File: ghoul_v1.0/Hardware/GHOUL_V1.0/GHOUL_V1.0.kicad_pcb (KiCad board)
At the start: 4 copper layers, 105.4 x 88.9 mm, 255 parts, among them M1 Motor_Servo, U1 Teensy4.1, U2 DS18S20, U3 Xbee, U4 TPS62133, U5 MS5607-02BA, U6 SAM-M8Q

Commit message: almost have V1.0 cleaned up
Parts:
- removed M1: Motor_Servo, Connector_JST:JST_EH_B4B-EH-A_1x04_P2.50mm_Vertical
- removed the REF** at (116.2, 69.2)
- removed REF**1, REF**10, REF**100, REF**101, REF**102, REF**103, REF**104, REF**105, REF**106, REF**107, REF**108, REF**109, REF**11, REF**110, REF**111, REF**112, REF**113, REF**114, REF**115, REF**117, REF**118, REF**119, REF**12, REF**120, REF**121, REF**122, REF**123, REF**125, REF**126, REF**127, REF**128, REF**129, REF**13, REF**130, REF**131, REF**133, REF**134, REF**135, REF**136, REF**137, REF**138, REF**139, REF**14, REF**140, REF**144, REF**145, REF**146, REF**147, REF**148, REF**149, REF**15, REF**150, REF**151, REF**152, REF**153, REF**154, REF**155, REF**156, REF**157, REF**158, REF**159, REF**16, REF**160, REF**161, REF**162, REF**163, REF**164, REF**165, REF**166, REF**167, REF**168, REF**169, REF**17, REF**170, REF**171, REF**172, REF**173, REF**174, REF**175, REF**176, REF**177, REF**178, REF**179, REF**18, REF**180, REF**181, REF**182, REF**183, REF**184, REF**185, REF**186, REF**187, REF**188, REF**189, REF**19, REF**190, REF**191, REF**192, REF**193, REF**194, REF**195, REF**196, REF**197, REF**198, REF**199, REF**2, REF**20, REF**200, REF**201, REF**202, REF**203, REF**204, REF**205, REF**206, REF**207, REF**208, REF**209, REF**21, REF**210, REF**211, REF**212, REF**213, REF**214, REF**215, REF**216, REF**217, REF**218, REF**219, REF**22, REF**220, REF**221, REF**222, REF**223, REF**224, REF**23, REF**24, REF**25, REF**26, REF**27, REF**28, REF**29, REF**3, REF**30, REF**31, REF**32, REF**33, REF**34, REF**35, REF**36, REF**37, REF**38, REF**39, REF**4, REF**40, REF**41, REF**42, REF**43, REF**44, REF**45, REF**46, REF**47, REF**48, REF**49, REF**5, REF**50, REF**51, REF**52, REF**53, REF**54, REF**55, REF**56, REF**57, REF**58, REF**59, REF**6, REF**60, REF**61, REF**62, REF**63, REF**64, REF**69, REF**7, REF**71, REF**72, REF**73, REF**74, REF**75, REF**76, REF**77, REF**78, REF**8, REF**80, REF**81, REF**82, REF**83, REF**84, REF**85, REF**86, REF**87, REF**88, REF**89, REF**9, REF**90, REF**91, REF**92, REF**94, REF**95, REF**96, REF**97, REF**98, REF**99: VIA_0.6mm, GHOULFootPrints:VIA_Stitch
- added M2: Motor_Servo, Connector_JST:JST_XH_B3B-XH-A_1x03_P2.50mm_Vertical, F.Cu at (167.6, 76.3)
- BT2: footprint ML414H_IV01E:SEIKO_ML414H_IV01E -> BPP_Lib:SEIKO_ML414H_IV01E
- C5, C7: footprint Capacitor_SMD:C_0201_0603Metric_Pad0.64x0.40mm_HandSolder -> Capacitor_SMD:C_0603_1608Metric_Pad1.08x0.95mm_HandSolder
- C8: value 1uf -> 1uF; footprint Capacitor_SMD:C_0201_0603Metric_Pad0.64x0.40mm_HandSolder -> Capacitor_SMD:C_0603_1608Metric_Pad1.08x0.95mm_HandSolder
- J1: renamed from Power Input1; value Conn_01x02 -> XT30
- J2: renamed from Cut-Down2; value NichromeConnector -> Conn_01x02
- J3: renamed from Cut-Down1; value NichromeConnector -> Conn_01x02
- R10: footprint Resistor_SMD:R_0201_0603Metric_Pad0.64x0.40mm_HandSolder -> Resistor_SMD:R_0603_1608Metric_Pad0.98x0.95mm_HandSolder
- R11: renamed from 0.3 Ohm Resistor1; value 03 -> 0.3
- R6, R7: value R220 -> 220; footprint Resistor_SMD:R_0201_0603Metric_Pad0.64x0.40mm_HandSolder -> Resistor_SMD:R_0603_1608Metric_Pad0.98x0.95mm_HandSolder
- U3: footprint GHOULFootPrints:XBee Explorer -> BPP_Lib:XBee Explorer
- U7: renamed from U1; footprint teensy.pretty-master:Teensy41 -> BPP_Lib:Teensy4_1
- moved J2 12.4 mm to (204.7, 106.7)
- moved J3 11.8 mm to (205.1, 117.5), turned to -90 degrees
- moved BT2 3.53 mm to (115.0, 128.6)
- moved R9 1.94 mm to (181.3, 104.7)
- moved C7 1.93 mm to (121.0, 84.5)
- moved R10 1.78 mm to (107.9, 127.3)
- moved R8 1.78 mm to (179.8, 104.7)
- moved D1 1.57 mm to (105.8, 125.9)
- moved C8 1.11 mm to (122.6, 86.6), turned to 0 degrees
- moved U2 0.99 mm to (169.5, 90.3)
- moved C4 0.99 mm to (181.7, 69.7)
- moved C6 0.99 mm to (179.8, 111.3)
- moved R11 0.99 mm to (196.6, 126.7)
- moved R5 0.99 mm to (183.5, 69.7)
- moved REF** 0.99 mm to (126.9, 139.9)
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- renumbered LM1084-ADJ1 to U1
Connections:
- net Feedback renamed /feedback
- net GPSRx renamed /GPS_RX
- net GPSTx renamed /GPS_TX
- net Nic1 renamed /nic1
- net Nic2 renamed /nic2
- net RTC_BATT renamed /RTC_BATT
- net Temp_Data renamed /Temp_Data
- net Vdiv renamed /Vdiv
- net Xbee DIn renamed /xbee_in
- net Xbee DOut renamed /xbee_out
- C8 pad 1: Net-(BT2-+) -> GND
- C8 pad 2: GND -> Net-(BT2-+)
- J2 pad 1: Net-(Cut-Down2-In) -> Net-(J2-Pin_1)
- J2 pad 2: Net-(Cut-Down1-In) -> Net-(J2-Pin_2)
- J3 pad 1: Net-(Cut-Down1-In) -> Net-(J2-Pin_1)
- J3 pad 2: Net-(Cut-Down1-Out) -> Net-(J3-Pin_2)
- MOSFET1 pad 2: Net-(Cut-Down1-Out) -> Net-(J2-Pin_2)
- MOSFET2 pad 2: Net-(Cut-Down2-In) -> Net-(J3-Pin_2)
- R11 pad 1: Net-(Cut-Down1-In) -> Net-(J2-Pin_1)
- R8 pad 1: Baro_SDA -> /SCL
- R9 pad 2: Baro_SCL -> /SDA
- U1 pad 1: Net-(Cut-Down1-In) -> Net-(J2-Pin_1)
- U5 pad 7: Baro_SDA -> /SDA
- U5 pad 8: Baro_SCL -> /SCL
- U7 pad 34: unconnected-(U1-GND-Pad34) -> GND
- U7 pad 38: Baro_SCL -> /SCL
- U7 pad 39: Baro_SDA -> /SDA
- U7 pad 4: Servo PWM -> Net-(M2-PWM)
- U7 pad 40: SDA -> unconnected-(U7-18_A4_SDA-Pad40)
- U7 pad 41: SCL -> unconnected-(U7-19_A5_SCL-Pad41)
- U7 pad 47: unconnected-(U1-GND-Pad47) -> GND
- U7 pad 52: unconnected-(U1-GND-Pad52) -> GND
- U7 pad 58: unconnected-(U1-GND-Pad58) -> GND
- U7 pad 59: unconnected-(U1-GND-Pad59) -> GND
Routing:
- net Net-(M2-PWM): track 0.00 -> 26.0 mm
- net Servo PWM: track 22.8 -> 0.00 mm
- net Baro_SDA: track 14.8 -> 0.00 mm
- net /SDA: track 0.00 -> 14.7 mm
- net /SCL: track 0.00 -> 11.2 mm
- net Baro_SCL: track 10.9 -> 0.00 mm
- net Net-(BT2-+): track 58.2 -> 61.4 mm, vias 3 -> 2
- net +3.3V: track 111.2 -> 108.1 mm, vias 6 -> 5
- net Net-(J3-Pin_2): track 0.00 -> 1.52 mm, vias 0 -> 3
- net Net-(Cut-Down2-In): track 1.52 -> 0.00 mm, vias 3 -> 0
- net /GPS_TX: track 31.4 -> 30.8 mm
- net /Temp_Data: track 34.7 -> 34.2 mm
- net Net-(U6-RXD): track 27.1 -> 26.6 mm
- net Net-(U6-TXD): track 27.0 -> 26.5 mm
- added copper zone on F.Cu, net Net-(J2-Pin_1)
- added copper zone on F.Cu, net Net-(J2-Pin_2)
- added copper zone on F.Cu, net Net-(J3-Pin_2)
- added copper zone on In2.Cu, net Net-(J3-Pin_2)
- removed copper zone on F.Cu, net Net-(BT2-+)
- removed copper zone on F.Cu, net Net-(Cut-Down1-In)
- removed copper zone on F.Cu, net Net-(Cut-Down1-Out)
- removed copper zone on F.Cu, net Net-(Cut-Down2-In)
- removed copper zone on In2.Cu, net Net-(Cut-Down2-In)
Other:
- board size 105.4 x 88.9 mm -> 104.1 x 88.9 mm

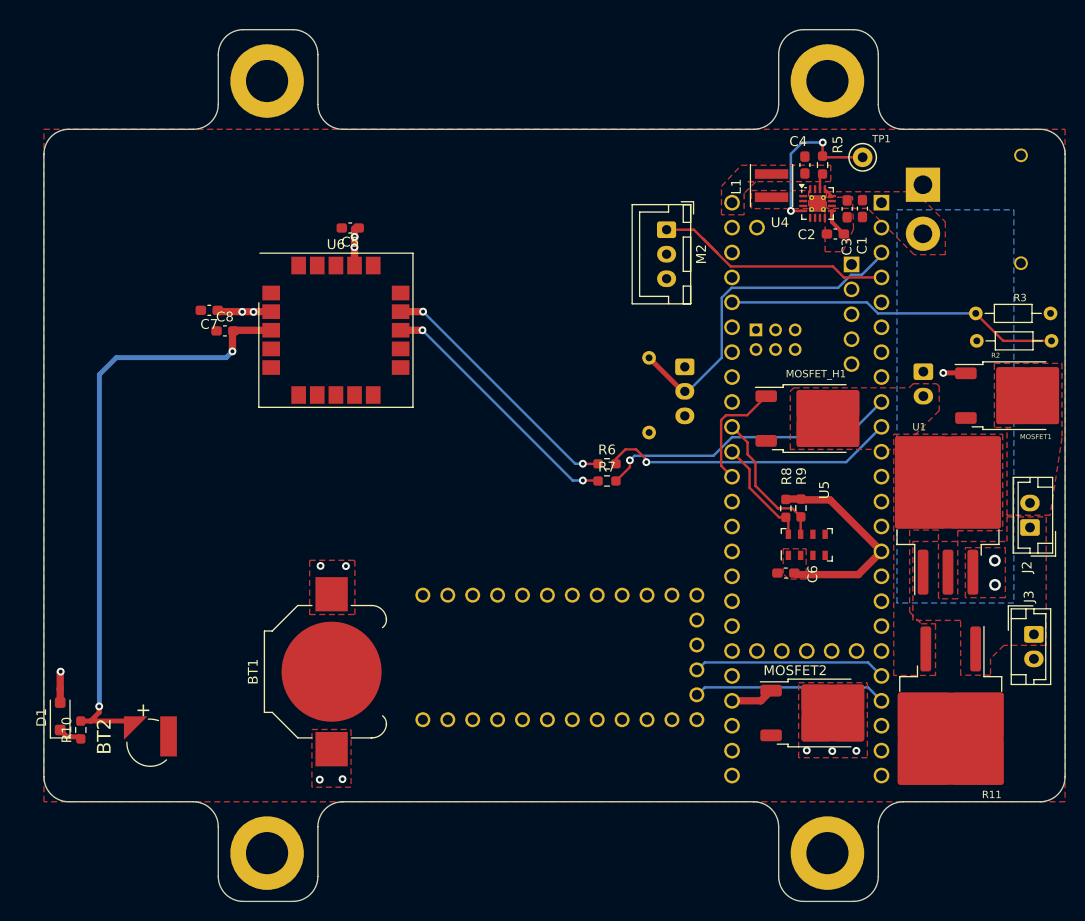
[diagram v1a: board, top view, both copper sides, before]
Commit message: switched GPS received, added via stitching, axial R to SMD
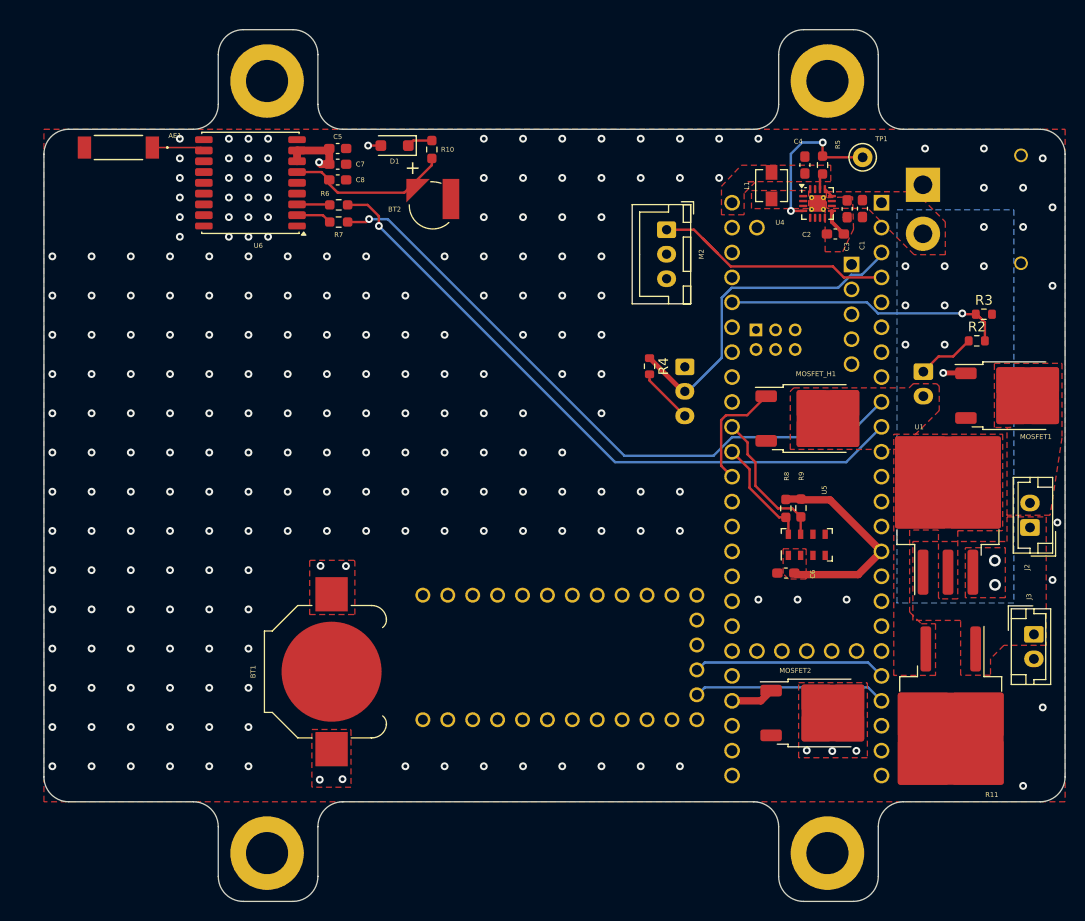
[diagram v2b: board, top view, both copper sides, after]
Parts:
- added AE1: 1575AT43A0040001E, BPP_Lib:ANT_1575AT_JOT-M, F.Cu at (111.7, 67.9)
- C5: value 1uf -> 10uf
- L1: footprint Inductor_SMD:L_Coilcraft_XxL4040 -> Inductor_SMD:L_Vishay_IHLP-1212
- R2, R3: footprint Resistor_THT:R_Axial_DIN0204_L3.6mm_D1.6mm_P7.62mm_Horizontal -> Resistor_SMD:R_0603_1608Metric
- R4: footprint Resistor_THT:R_Axial_DIN0204_L3.6mm_D1.6mm_P7.62mm_Horizontal -> Resistor_SMD:R_0603_1608Metric; moved to F.Cu
- U6: value SAM-M8Q -> MAX-M10S; footprint RF_GPS:ublox_SAM-M8Q -> RF_GPS:ublox_MAX
- moved R10 69.2 mm to (143.7, 68.1), turned to -90 degrees
- moved D1 67.5 mm to (139.9, 67.7), turned to 180 degrees
- moved BT2 61.9 mm to (143.8, 73.8)
- moved R6 38.0 mm to (134.2, 73.8)
- moved R7 38.0 mm to (134.2, 75.5)
- moved C7 19.8 mm to (134.1, 69.6), turned to 0 degrees
- moved C8 19.2 mm to (134.1, 71.2), turned to 180 degrees
- moved U6 17.4 mm to (125.2, 71.5), turned to 180 degrees
- moved C5 8.21 mm to (134.1, 68.0), turned to 0 degrees
- moved R4 0.86 mm to (165.9, 90.2)
- moved R3 0.83 mm to (200.0, 84.9)
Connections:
- U6 pad 11: GND -> Net-(AE1-A)
- U6 pad 12: unconnected-(U6-SCL-Pad12) -> GND
- U6 pad 13: Net-(U6-TXD) -> unconnected-(U6-LNA_EN-Pad13)
- U6 pad 14: Net-(U6-RXD) -> unconnected-(U6-VCC_RF-Pad14)
- U6 pad 15: GND -> unconnected-(U6-VIO_SEL-Pad15)
- U6 pad 16: GND -> unconnected-(U6-SDA-Pad16)
- U6 pad 17: +3.3V -> unconnected-(U6-SCL-Pad17)
- U6 pad 2: +3.3V -> Net-(U6-TXD)
- U6 pad 3: Net-(BT2-+) -> Net-(U6-RXD)
- U6 pad 4: GND -> unconnected-(U6-TIMEPULSE-Pad4)
- U6 pad 5: GND -> unconnected-(U6-EXTINT-Pad5)
- U6 pad 6: GND -> Net-(BT2-+)
- U6 pad 7: unconnected-(U6-TIMEPULSE-Pad7) -> +3.3V
- U6 pad 8: unconnected-(U6-~{SAFEBOOT}-Pad8) -> +3.3V
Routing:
- net +3.3V: track 108.1 -> 36.1 mm, vias 5 -> 2
- net Net-(BT2-+): track 61.4 -> 16.7 mm, vias 2 -> 0
- net /GPS_RX: track 30.2 -> 67.4 mm
- net /GPS_TX: track 30.8 -> 66.8 mm
- net Net-(U6-RXD): track 26.6 -> 3.36 mm, vias 2 -> 0
- net Net-(U6-TXD): track 26.5 -> 3.63 mm, vias 2 -> 0
- net +BATT: track 1.01 -> 6.93 mm
- net Net-(AE1-A): track 0.00 -> 5.37 mm
- net /Vdiv: track 34.2 -> 29.4 mm, vias 0 -> 1
- net GND: vias 0 -> 228
